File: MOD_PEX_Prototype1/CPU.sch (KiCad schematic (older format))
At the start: 17 parts, among them P2 HEADER_5X2, P3 HEADER_5X2, U1 LPC111X_LQFP48, X1 10MHz

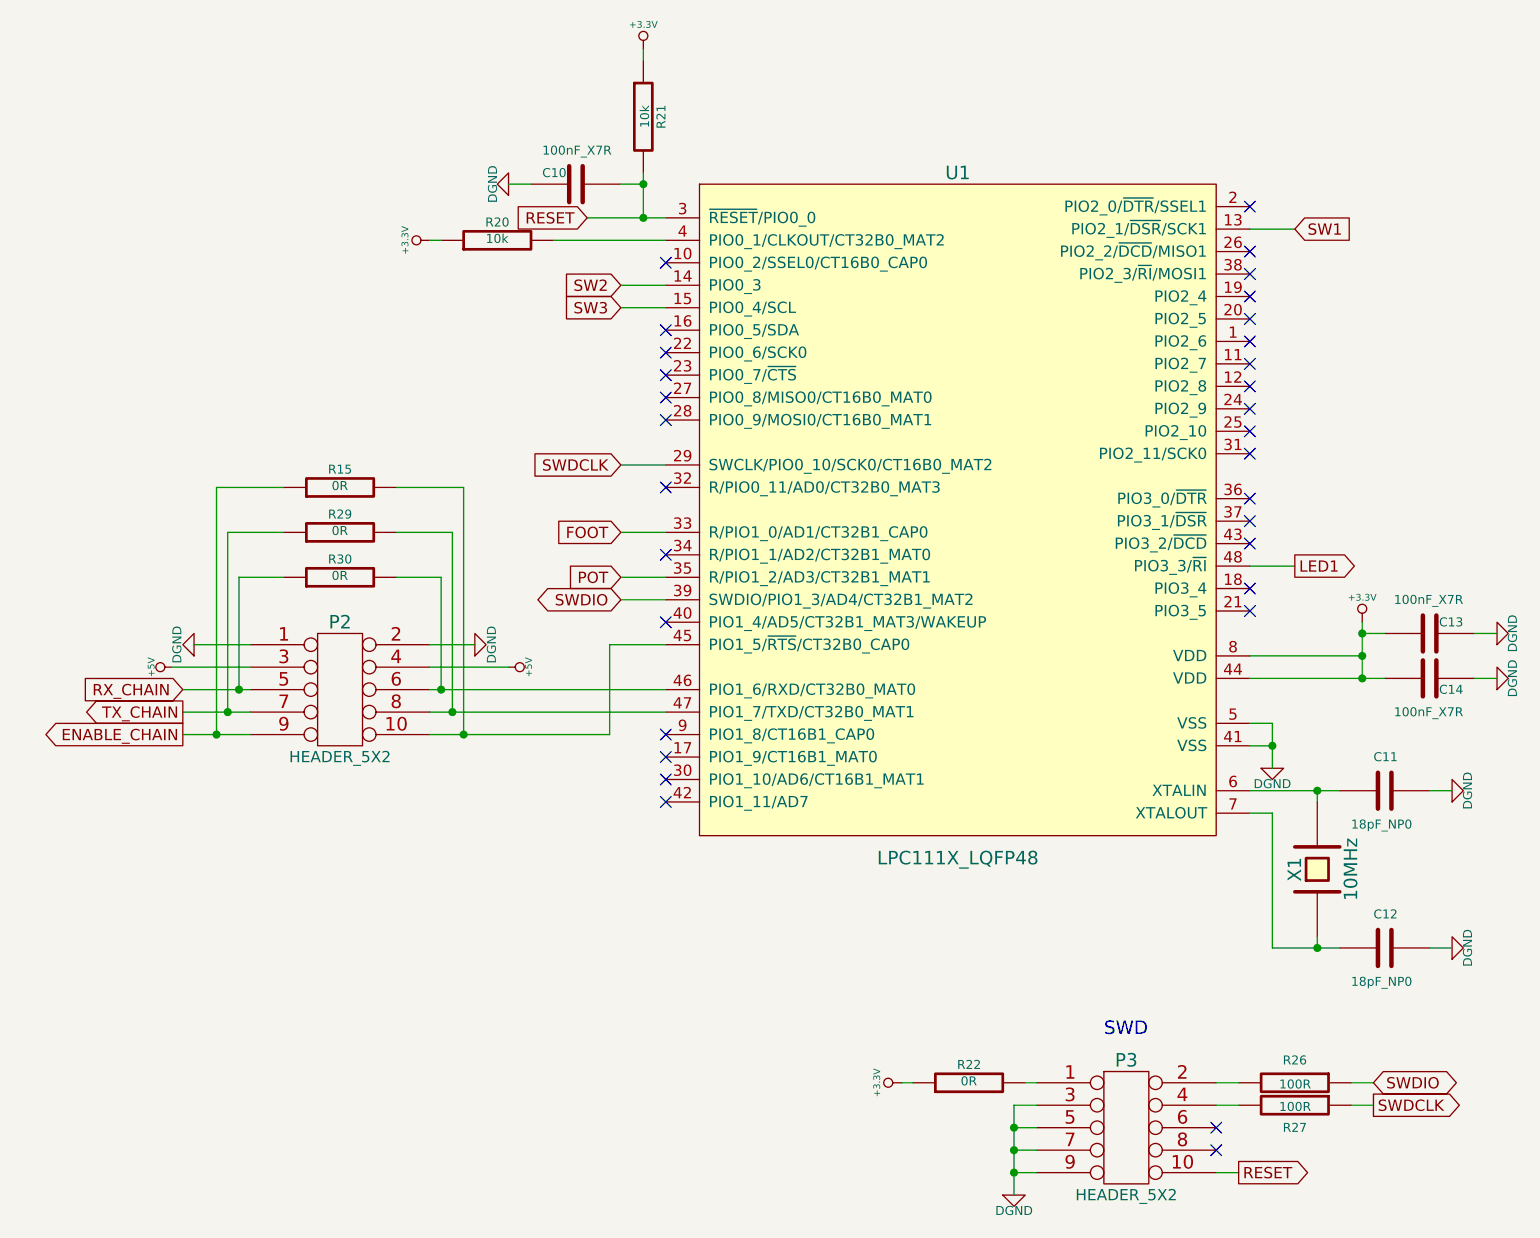
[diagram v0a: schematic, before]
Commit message: updating control chain circuit
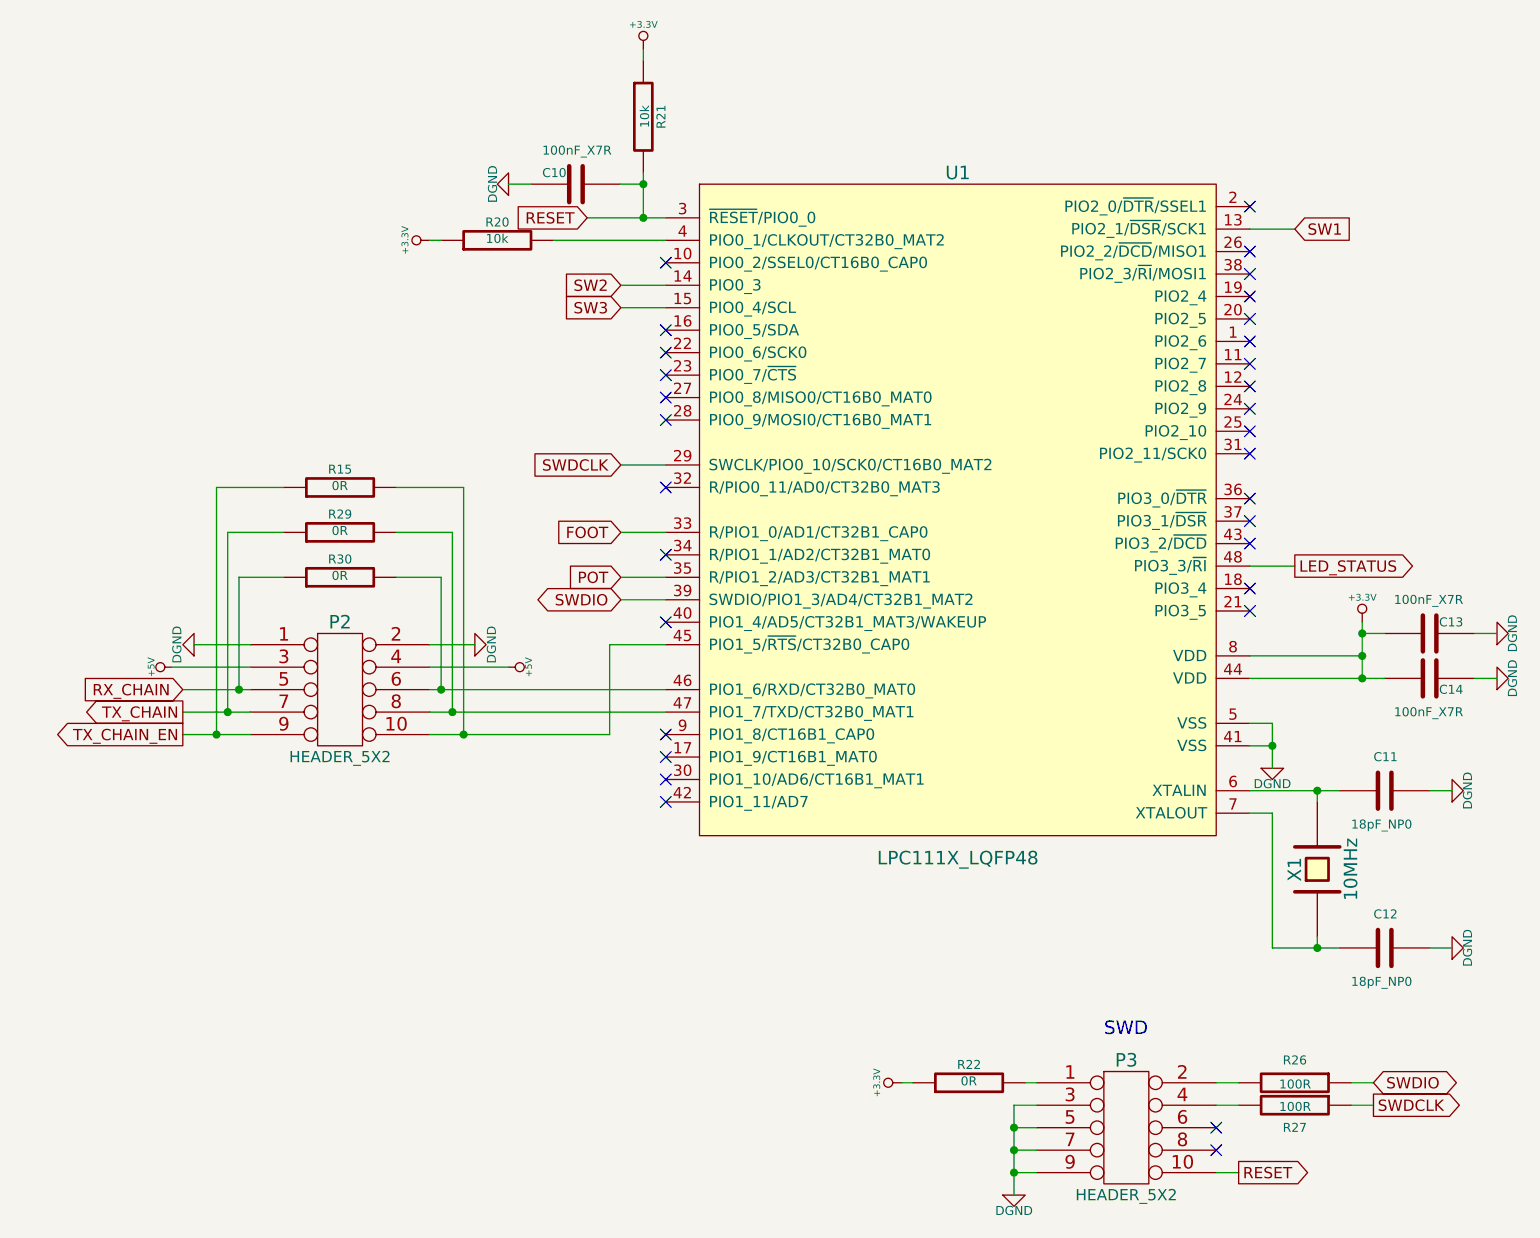
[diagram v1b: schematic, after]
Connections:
- net ENABLE_CHAIN renamed TX_CHAIN_EN
- net LED1 renamed LED_STATUS
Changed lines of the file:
@@
 $EndComp
 $Comp
-L DGND #PWR050
+L DGND #PWR060
 U 1 1 548B6D7E
 P 7050 4450
-F 0 "#PWR050" H 7050 4450 40  0001 C CNN
+F 0 "#PWR060" H 7050 4450 40  0001 C CNN
 F 1 "DGND" H 7050 4380 40  0000 C CNN
 F 2 "" H 7050 4450 60  0000 C CNN
@@
 $EndComp
 $Comp
-L DGND #PWR051
+L DGND #PWR061
 U 1 1 548B6D8B
 P 8050 4050
-F 0 "#PWR051" H 8050 4050 40  0001 C CNN
+F 0 "#PWR061" H 8050 4050 40  0001 C CNN
 F 1 "DGND" H 8050 3980 40  0000 C CNN
 F 2 "" H 8050 4050 60  0000 C CNN
@@
 $EndComp
 $Comp
-L DGND #PWR052
+L DGND #PWR062
 U 1 1 548B6D91
 P 8050 3850
-F 0 "#PWR052" H 8050 3850 40  0001 C CNN
+F 0 "#PWR062" H 8050 3850 40  0001 C CNN
 F 1 "DGND" H 8050 3780 40  0000 C CNN
 F 2 "" H 8050 3850 60  0000 C CNN
@@
 $EndComp
 $Comp
-L +3.3V #PWR053
+L +3.3V #PWR063
 U 1 1 548B6D97
 P 7450 3800
-F 0 "#PWR053" H 7450 3760 30  0001 C CNN
+F 0 "#PWR063" H 7450 3760 30  0001 C CNN
 F 1 "+3.3V" H 7450 3910 30  0000 C CNN
 F 2 "" H 7450 3800 60  0000 C CNN
@@
 $EndComp
 $Comp
-L DGND #PWR054
+L DGND #PWR064
 U 1 1 548B6DAB
 P 7850 5250
-F 0 "#PWR054" H 7850 5250 40  0001 C CNN
+F 0 "#PWR064" H 7850 5250 40  0001 C CNN
 F 1 "DGND" H 7850 5180 40  0000 C CNN
 F 2 "" H 7850 5250 60  0000 C CNN
@@
 $EndComp
 $Comp
-L DGND #PWR055
+L DGND #PWR065
 U 1 1 548B6DB1
 P 7850 4550
-F 0 "#PWR055" H 7850 4550 40  0001 C CNN
+F 0 "#PWR065" H 7850 4550 40  0001 C CNN
 F 1 "DGND" H 7850 4480 40  0000 C CNN
 F 2 "" H 7850 4550 60  0000 C CNN
@@
 $EndComp
 $Comp
-L DGND #PWR056
+L DGND #PWR066
 U 1 1 548B6DCC
 P 3650 1850
-F 0 "#PWR056" H 3650 1850 40  0001 C CNN
+F 0 "#PWR066" H 3650 1850 40  0001 C CNN
 F 1 "DGND" H 3650 1780 40  0000 C CNN
 F 2 "" H 3650 1850 60  0000 C CNN
@@
 $EndComp
 $Comp
-L +3.3V #PWR057
+L +3.3V #PWR067
 U 1 1 548B6DD2
 P 4250 1250
-F 0 "#PWR057" H 4250 1210 30  0001 C CNN
+F 0 "#PWR067" H 4250 1210 30  0001 C CNN
 F 1 "+3.3V" H 4250 1360 30  0000 C CNN
 F 2 "" H 4250 1250 60  0000 C CNN
@@
 SWDCLK
 $Comp
-L DGND #PWR058
+L DGND #PWR068
 U 1 1 548B6DE3
 P 5900 6350
-F 0 "#PWR058" H 5900 6350 40  0001 C CNN
+F 0 "#PWR068" H 5900 6350 40  0001 C CNN
 F 1 "DGND" H 5900 6280 40  0000 C CNN
 F 2 "" H 5900 6350 60  0000 C CNN
@@
 NoConn ~ 6800 6150
 Text GLabel 7150 3550 2    50   Output ~ 0
-LED1
+LED_STATUS
 NoConn ~ 6950 3650
 NoConn ~ 6950 3750
@@
 TX_CHAIN
 $Comp
-L +5V #PWR059
+L +5V #PWR069
 U 1 1 548B6DF3
 P 2150 4000
-F 0 "#PWR059" H 2150 4090 20  0001 C CNN
+F 0 "#PWR069" H 2150 4090 20  0001 C CNN
 F 1 "+5V" H 2150 4090 30  0000 C CNN
 F 2 "" H 2150 4000 60  0000 C CNN
@@
 $EndComp
 $Comp
-L DGND #PWR060
+L DGND #PWR070
 U 1 1 548B6DF9
 P 2250 3900
-F 0 "#PWR060" H 2250 3900 40  0001 C CNN
+F 0 "#PWR070" H 2250 3900 40  0001 C CNN
 F 1 "DGND" H 2250 3825 40  0000 C CNN
 F 2 "" H 2250 3900 60  0000 C CNN
@@
 $EndComp
 $Comp
-L +3.3V #PWR061
+L +3.3V #PWR071
 U 1 1 548B6E06
 P 3300 2100
-F 0 "#PWR061" H 3300 2060 30  0001 C CNN
+F 0 "#PWR071" H 3300 2060 30  0001 C CNN
 F 1 "+3.3V" H 3300 2210 30  0000 C CNN
 F 2 "" H 3300 2100 60  0000 C CNN
@@
 	6000 5850 5950 5850
 $Comp
-L +3.3V #PWR062
+L +3.3V #PWR072
 U 1 1 548B6E58
 P 5400 5850
-F 0 "#PWR062" H 5400 5810 30  0001 C CNN
+F 0 "#PWR072" H 5400 5810 30  0001 C CNN
 F 1 "+3.3V" H 5400 5960 30  0000 C CNN
 F 2 "" H 5400 5850 60  0000 C CNN
@@
 NoConn ~ 4350 4600
 Text GLabel 2200 4300 0    50   Output ~ 0
-ENABLE_CHAIN
+TX_CHAIN_EN
 Wire Wire Line
 	2200 4300 2500 4300
@@
 $EndComp
 $Comp
-L DGND #PWR063
+L DGND #PWR073
 U 1 1 548B6E8F
 P 3500 3900
-F 0 "#PWR063" H 3500 3900 40  0001 C CNN
+F 0 "#PWR073" H 3500 3900 40  0001 C CNN
 F 1 "DGND" H 3500 3825 40  0000 C CNN
 F 2 "" H 3500 3900 60  0000 C CNN
@@
 $EndComp
 $Comp
-L +5V #PWR064
+L +5V #PWR074
 U 1 1 548B6E95
 P 3650 4000
-F 0 "#PWR064" H 3650 4090 20  0001 C CNN
+F 0 "#PWR074" H 3650 4090 20  0001 C CNN
 F 1 "+5V" H 3650 4090 30  0000 C CNN
 F 2 "" H 3650 4000 60  0000 C CNN
